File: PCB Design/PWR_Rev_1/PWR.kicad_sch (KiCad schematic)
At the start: 61 parts, among them J1 Conn_01x24_Pin, J2 Conn_01x24_Pin, U1 LMR33630ADDA, U2 LMR33630ADDA, U3 LMR33630ADDA

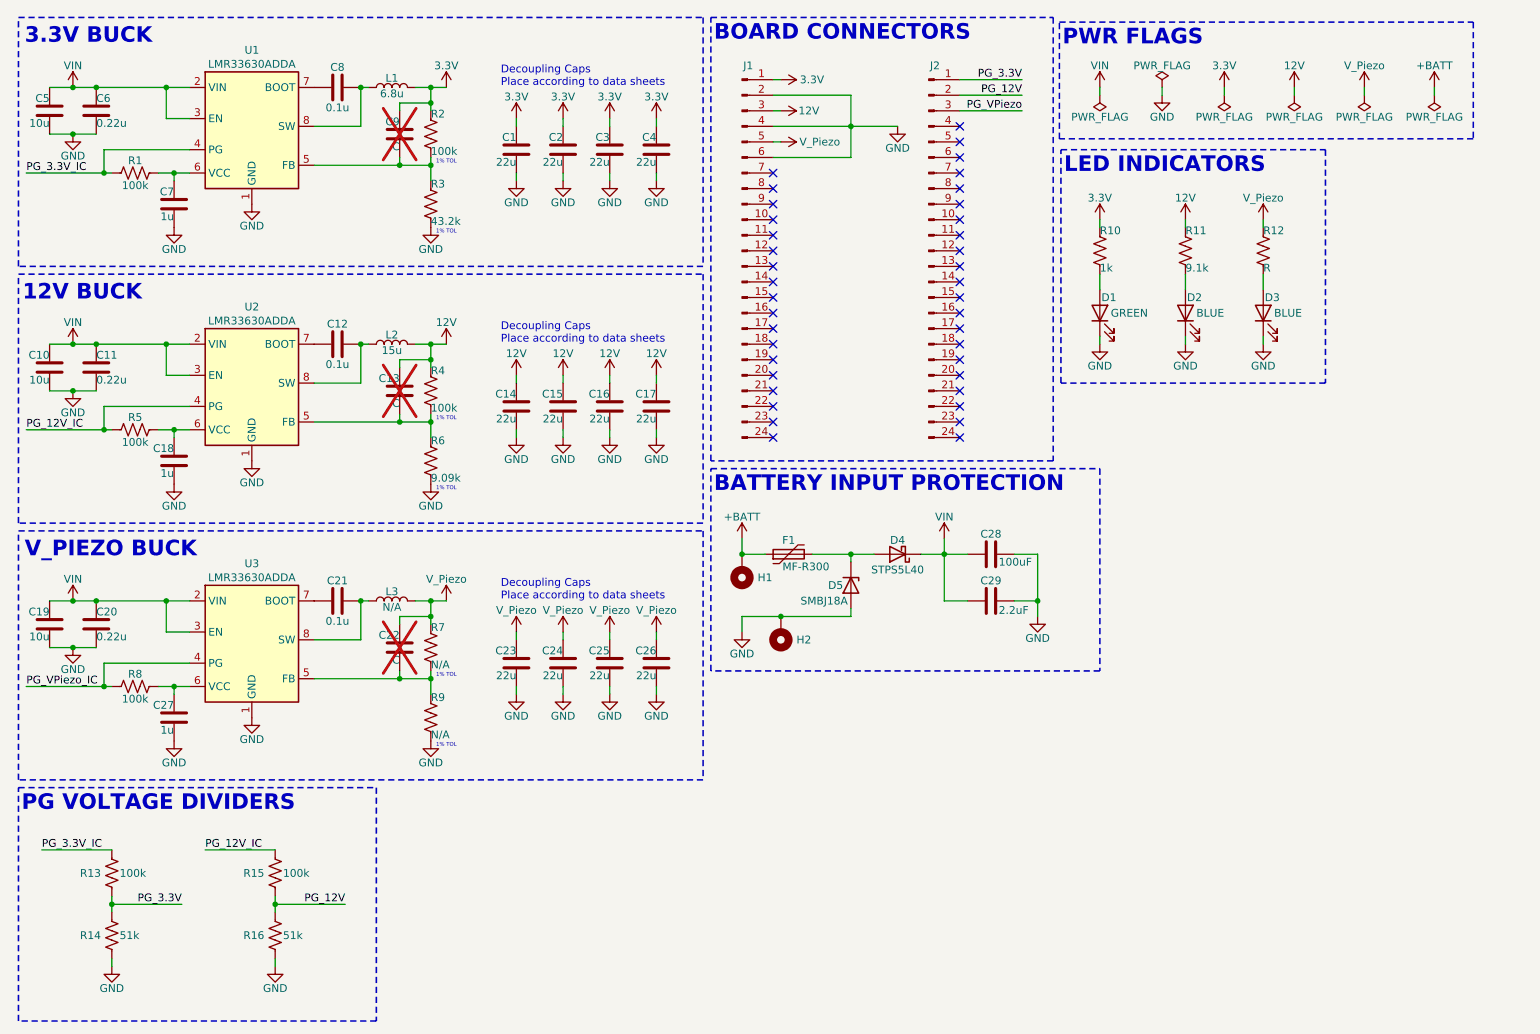
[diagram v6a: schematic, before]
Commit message: Added Boost for V_Piezo
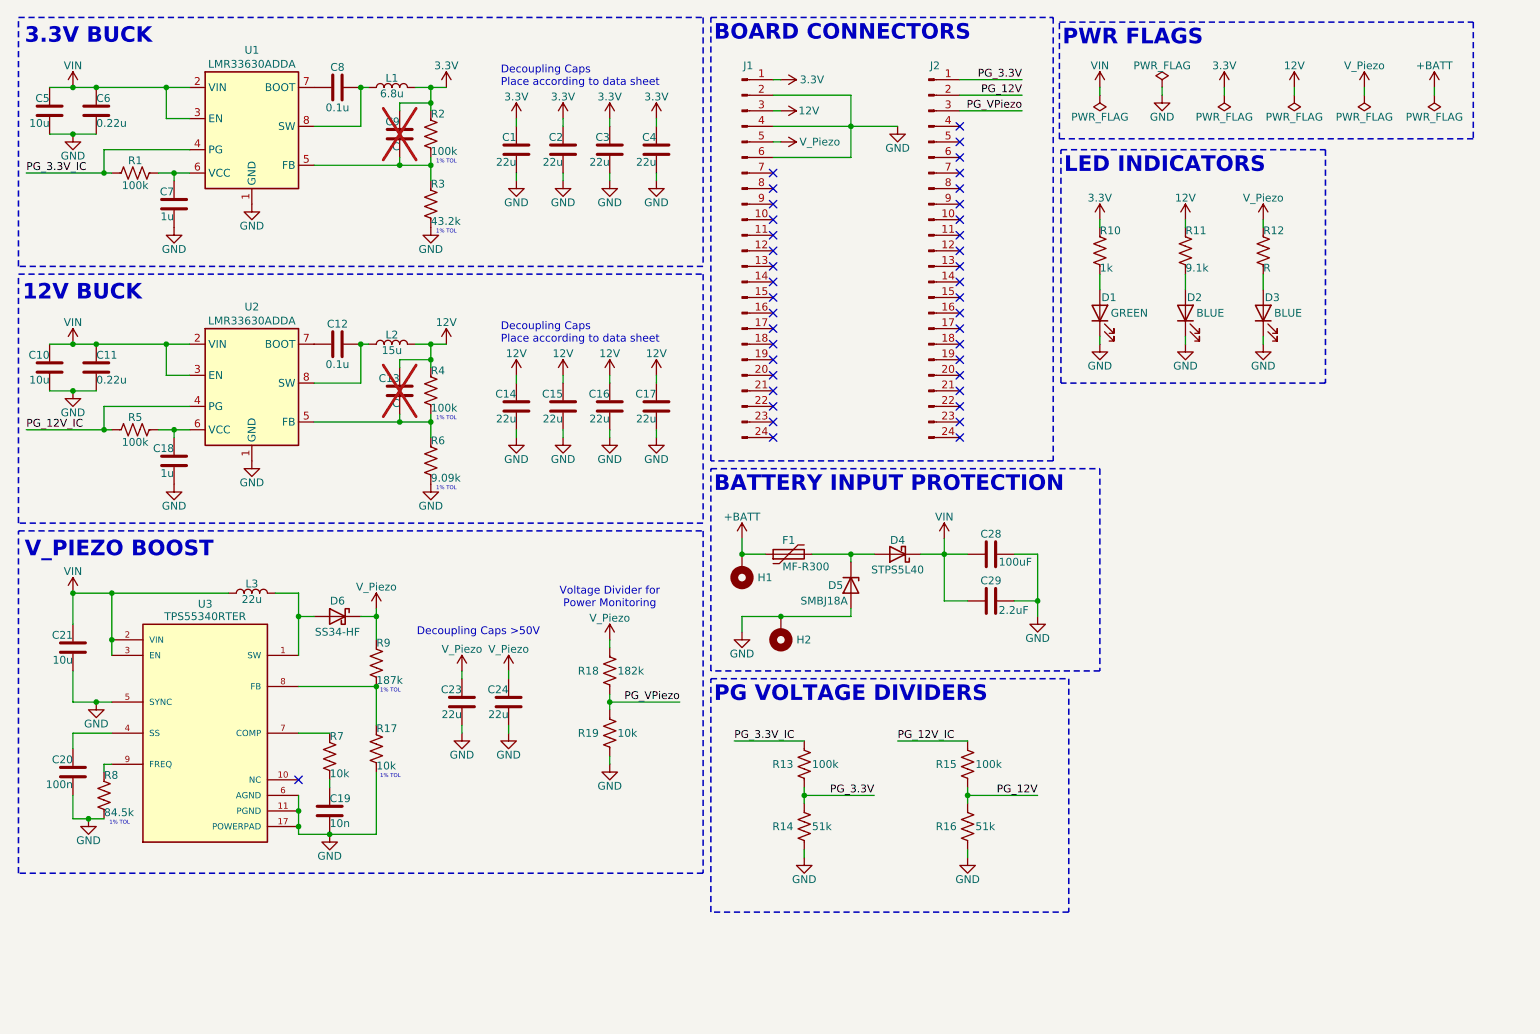
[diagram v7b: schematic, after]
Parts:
- removed C22: C, Capacitor_SMD:C_0603_1608Metric, symbol Device:C
- removed C25, C26: 22u, Capacitor_SMD:C_1210_3225Metric, symbol Device:C
- removed C27: 1u, Capacitor_SMD:C_0603_1608Metric, symbol Device:C
- removed U3: LMR33630ADDA, PWR_Library:Texas_HSOP-8-1EP_3.9x4.9mm_P1.27mm_ThermalVias, symbol Regulator_Switching:LMR33630ADDA
- added D6: SS34-HF, Diode_SMD:D_SMA, symbol Diode:DSB2810
- added R17, R19: 10k, Resistor_SMD:R_0603_1608Metric, symbol Device:R_US
- added R18: 182k, Resistor_SMD:R_0603_1608Metric, symbol Device:R_US
- added U3: TPS55340RTER, PWR_Library:QFN50P300X300X80-17N, symbol PWR_Library:TPS55340RTER
- C19: value 10u -> 10n; footprint Capacitor_SMD:C_1210_3225Metric -> Capacitor_SMD:C_0603_1608Metric
- C20: value 0.22u -> 100n
- C21: value 0.1u -> 10u; footprint Capacitor_SMD:C_0603_1608Metric -> Capacitor_SMD:C_1206_3216Metric
- L3: value N/A -> 22u; footprint PWR_Library:L_Wuerth_MAPI-5030 -> Inductor_SMD:L_Bourns_SDR0604
- R7: value N/A -> 10k
- R8: value 100k -> 84.5k
- R9: value N/A -> 187k
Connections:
- net PG_VPiezo_IC is gone; now on net GND: R8.1
- net GND: now also C21.2, R17.1, R19.1, U3.11 (PGND), U3.12 (PGND), U3.13 (PGND), U3.17 (POWERPAD), U3.5 (SYNC), U3.6 (AGND); no longer R9.1
- net PG_VPiezo: now also R18.1, R19.2
- net VIN: now also C21.1, L3.1, U3.2 (VIN), U3.3 (EN); no longer C19.1, C20.1
- net V_Piezo: now also R9.2, D6.1 (K), R18.2; no longer L3.2, R7.2
- net at R7.1: now also C19.1; no longer R9.2
- net at R8.2: now also U3.9 (FREQ)
- new net: D6.2 (A), L3.2, U3.1 (SW), U3.15 (SW), U3.16 (SW)
- new net: C20.1, U3.4 (SS)
- new net: R7.2, U3.7 (COMP)
- new net: R17.2, R9.1, U3.8 (FB)
- new net NC: U3.10 (NC), U3.14 (NC)
- no-connect marks 39 -> 40
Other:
- note added: "Decoupling Caps >50V"
- note added: "Decoupling Caps Place according to data sheet"
- note added: "V_PIEZO BOOST"
- note added: "Voltage Divider for Power Monitoring"
- note removed: "Decoupling Caps Place according to data sheets"
- note removed: "V_PIEZO BUCK"
- moved on the sheet: C23, C24, R13, R14, R15, R16

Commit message: Updated to KiCAD 10 and exported BOM
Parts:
- U3: Package WQFN-16 Texas Instruments -> (none)
